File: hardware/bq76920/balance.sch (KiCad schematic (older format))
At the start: 32 parts, among them Q4 NTR3C21NZ, Q5 NTR3C21NZ, Q6 NTR3C21NZ, Q7 NTR3C21NZ, Q8 NTR3C21NZ

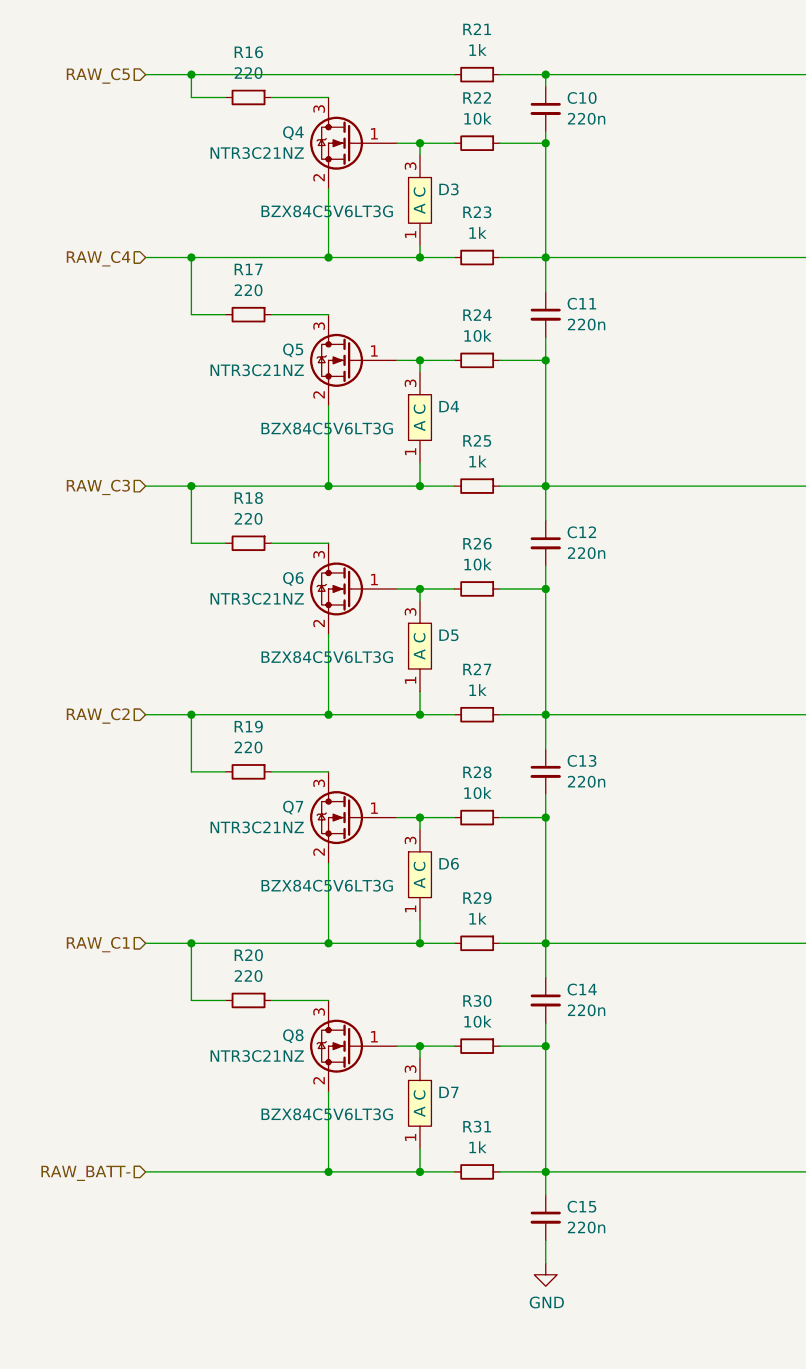
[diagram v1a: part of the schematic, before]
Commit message: update cpu and reduce BOM
Signed-off-by: Ene Alexandru <ene.alexandru@gmail.com>
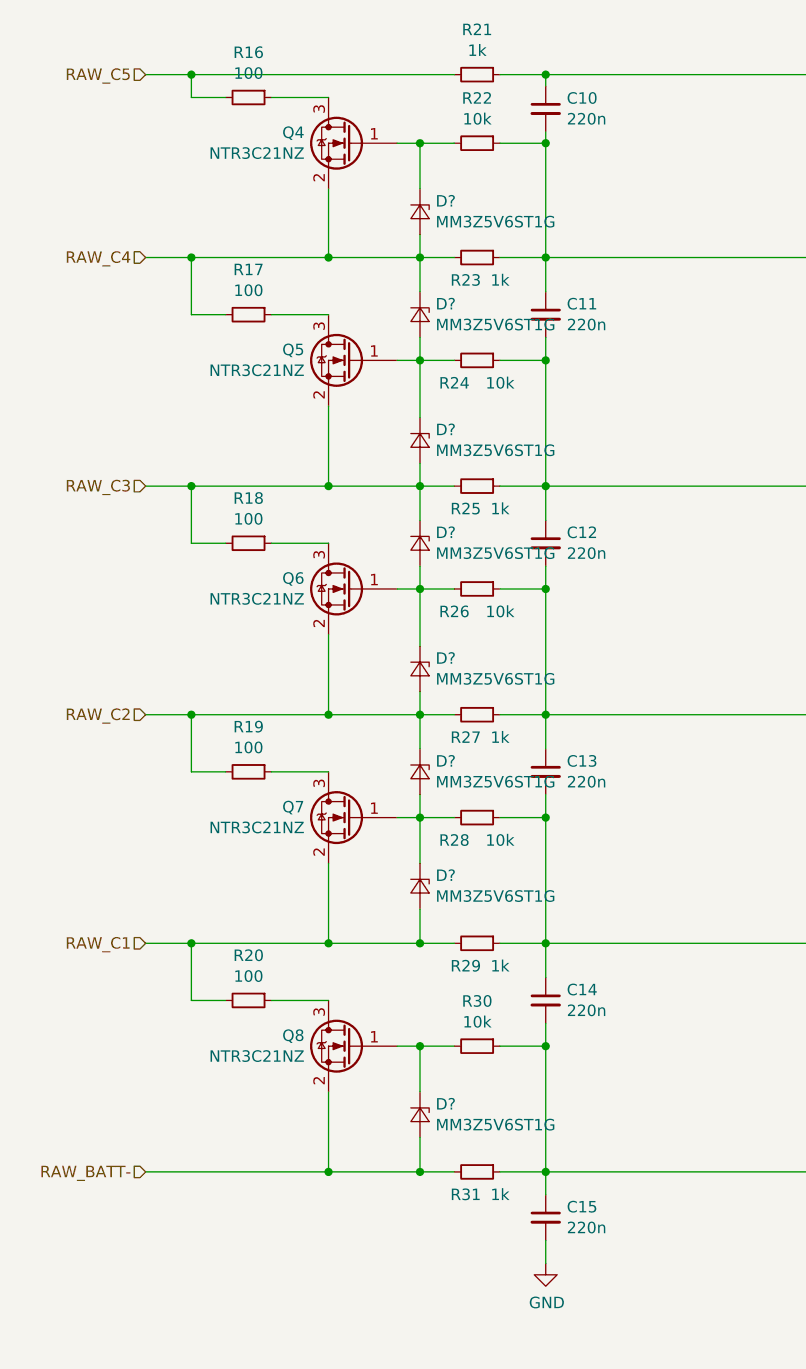
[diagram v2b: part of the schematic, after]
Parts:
- removed D3, D4, D5, D6, D7: BZX84C5V6LT3G, Package_TO_SOT_SMD:SOT-23, symbol bq76920-rescue:BZX84C5V6LT3G-bq769xx
- added D? (x8): MM3Z5V6ST1G, Diode_SMD:D_SOD-323, symbol Device:D_Zener_Small
- R16, R17, R18, R19, R20: value 220 -> 100
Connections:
- net RAW_BATT-: now also D?.2 (A)
- net RAW_C1: now also D?.2 (A)
- net RAW_C2: now also D?.1 (K), D?.2 (A)
- net RAW_C3: now also D?.1 (K), D?.2 (A)
- net RAW_C4: now also D?.1 (K), D?.2 (A)
- net at Q4.1 (G), R22.2: now also D?.1 (K)
- net at Q5.1 (G), R24.2: now also D?.1 (K), D?.2 (A)
- net at Q6.1 (G), R26.2: now also D?.1 (K), D?.2 (A)
- net at Q7.1 (G), R28.2: now also D?.1 (K), D?.2 (A)
- net at Q8.1 (G), R30.2: now also D?.1 (K)
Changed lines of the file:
@@
-$EndComp
-$Comp
-L bq76920-rescue:BZX84C5V6LT3G-bq769xx D3
-U 1 1 5D445057
-P 3700 1200
-AR Path="/5D445057" Ref="D3"  Part="1"
-AR Path="/5D4426A3/5D445057" Ref="D3"  Part="1"
-F 0 "D3" H 3778 1046 50  0000 L CNN
-F 1 "BZX84C5V6LT3G" H 3000 950 50  0000 L CNN
-F 2 "Package_TO_SOT_SMD:SOT-23" H 3700 1200 50  0001 C CNN
-F 3 "" H 3700 1200 50  0001 C CNN
-	1    3700 1200
-	1    0    0    -1
 $EndComp
 $Comp
@@
 P 2950 950
 F 0 "R16" V 2754 950 50  0000 C CNN
-F 1 "220" V 2845 950 50  0000 C CNN
+F 1 "100" V 2845 950 50  0000 C CNN
 F 2 "Resistor_SMD:R_1206_3216Metric_Pad1.42x1.75mm_HandSolder" H 2950 950 50  0001 C CNN
 F 3 "~" H 2950 950 50  0001 C CNN
@@
 U 1 1 5D44C6D5
 P 3950 1650
-F 0 "R23" V 3754 1650 50  0000 C CNN
-F 1 "1k" V 3845 1650 50  0000 C CNN
+F 0 "R23" V 4050 1600 50  0000 C CNN
+F 1 "1k" V 4050 1750 50  0000 C CNN
 F 2 "Resistor_SMD:R_0805_2012Metric_Pad1.15x1.40mm_HandSolder" H 3950 1650 50  0001 C CNN
 F 3 "~" H 3950 1650 50  0001 C CNN
@@
 Wire Wire Line
 	4250 850  4050 850
-Wire Wire Line
-	3700 1600 3700 1650
 Connection ~ 3700 1650
 Wire Wire Line
@@
 Wire Wire Line
 	3600 1150 3700 1150
-Wire Wire Line
-	3700 1150 3700 1200
 Connection ~ 3700 1150
 Wire Wire Line
@@
 P 2950 1900
 F 0 "R17" V 2754 1900 50  0000 C CNN
-F 1 "220" V 2845 1900 50  0000 C CNN
+F 1 "100" V 2845 1900 50  0000 C CNN
 F 2 "Resistor_SMD:R_1206_3216Metric_Pad1.42x1.75mm_HandSolder" H 2950 1900 50  0001 C CNN
 F 3 "~" H 2950 1900 50  0001 C CNN
@@
 $EndComp
 $Comp
-L bq76920-rescue:BZX84C5V6LT3G-bq769xx D4
-U 1 1 5D458C86
-P 3700 2150
-AR Path="/5D458C86" Ref="D4"  Part="1"
-AR Path="/5D4426A3/5D458C86" Ref="D4"  Part="1"
-F 0 "D4" H 3778 1996 50  0000 L CNN
-F 1 "BZX84C5V6LT3G" H 3000 1900 50  0000 L CNN
-F 2 "Package_TO_SOT_SMD:SOT-23" H 3700 2150 50  0001 C CNN
-F 3 "" H 3700 2150 50  0001 C CNN
-	1    3700 2150
-	1    0    0    -1
-$EndComp
-$Comp
 L Device:R_Small R24
 U 1 1 5D4590AC
 P 3950 2100
-F 0 "R24" V 3754 2100 50  0000 C CNN
-F 1 "10k" V 3845 2100 50  0000 C CNN
+F 0 "R24" V 4050 2000 50  0000 C CNN
+F 1 "10k" V 4050 2200 50  0000 C CNN
 F 2 "Resistor_SMD:R_0805_2012Metric_Pad1.15x1.40mm_HandSolder" H 3950 2100 50  0001 C CNN
 F 3 "~" H 3950 2100 50  0001 C CNN
@@
 U 1 1 5D45948A
 P 3950 2650
-F 0 "R25" V 3754 2650 50  0000 C CNN
-F 1 "1k" V 3845 2650 50  0000 C CNN
+F 0 "R25" V 4050 2600 50  0000 C CNN
+F 1 "1k" V 4050 2750 50  0000 C CNN
 F 2 "Resistor_SMD:R_0805_2012Metric_Pad1.15x1.40mm_HandSolder" H 3950 2650 50  0001 C CNN
 F 3 "~" H 3950 2650 50  0001 C CNN
@@
 Wire Wire Line
 	3850 2100 3700 2100
-Wire Wire Line
-	3700 2150 3700 2100
 Connection ~ 3700 2100
 Wire Wire Line
@@
 P 2950 2900
 F 0 "R18" V 2754 2900 50  0000 C CNN
-F 1 "220" V 2845 2900 50  0000 C CNN
+F 1 "100" V 2845 2900 50  0000 C CNN
 F 2 "Resistor_SMD:R_1206_3216Metric_Pad1.42x1.75mm_HandSolder" H 2950 2900 50  0001 C CNN
 F 3 "~" H 2950 2900 50  0001 C CNN
@@
 $EndComp
 $Comp
-L bq76920-rescue:BZX84C5V6LT3G-bq769xx D5
-U 1 1 5D461225
-P 3700 3150
-AR Path="/5D461225" Ref="D5"  Part="1"
-AR Path="/5D4426A3/5D461225" Ref="D5"  Part="1"
-F 0 "D5" H 3778 2996 50  0000 L CNN
-F 1 "BZX84C5V6LT3G" H 3000 2900 50  0000 L CNN
-F 2 "Package_TO_SOT_SMD:SOT-23" H 3700 3150 50  0001 C CNN
-F 3 "" H 3700 3150 50  0001 C CNN
-	1    3700 3150
-	1    0    0    -1
-$EndComp
-$Comp
 L Device:R_Small R26
 U 1 1 5D46299B
 P 3950 3100
-F 0 "R26" V 3754 3100 50  0000 C CNN
-F 1 "10k" V 3845 3100 50  0000 C CNN
+F 0 "R26" V 4050 3000 50  0000 C CNN
+F 1 "10k" V 4050 3200 50  0000 C CNN
 F 2 "Resistor_SMD:R_0805_2012Metric_Pad1.15x1.40mm_HandSolder" H 3950 3100 50  0001 C CNN
 F 3 "~" H 3950 3100 50  0001 C CNN
@@
 U 1 1 5D462DC7
 P 3950 3650
-F 0 "R27" V 3754 3650 50  0000 C CNN
-F 1 "1k" V 3845 3650 50  0000 C CNN
+F 0 "R27" V 4050 3600 50  0000 C CNN
+F 1 "1k" V 4050 3750 50  0000 C CNN
 F 2 "Resistor_SMD:R_0805_2012Metric_Pad1.15x1.40mm_HandSolder" H 3950 3650 50  0001 C CNN
 F 3 "~" H 3950 3650 50  0001 C CNN
@@
 Wire Wire Line
 	3850 3100 3700 3100
-Wire Wire Line
-	3700 3150 3700 3100
 Connection ~ 3700 3100
 Wire Wire Line
@@
 P 2950 3900
 F 0 "R19" V 2754 3900 50  0000 C CNN
-F 1 "220" V 2845 3900 50  0000 C CNN
+F 1 "100" V 2845 3900 50  0000 C CNN
 F 2 "Resistor_SMD:R_1206_3216Metric_Pad1.42x1.75mm_HandSolder" H 2950 3900 50  0001 C CNN
 F 3 "~" H 2950 3900 50  0001 C CNN
@@
 $EndComp
 $Comp
-L bq76920-rescue:BZX84C5V6LT3G-bq769xx D6
-U 1 1 5D47B43C
-P 3700 4150
-AR Path="/5D47B43C" Ref="D6"  Part="1"
-AR Path="/5D4426A3/5D47B43C" Ref="D6"  Part="1"
-F 0 "D6" H 3778 3996 50  0000 L CNN
-F 1 "BZX84C5V6LT3G" H 3000 3900 50  0000 L CNN
-F 2 "Package_TO_SOT_SMD:SOT-23" H 3700 4150 50  0001 C CNN
-F 3 "" H 3700 4150 50  0001 C CNN
-	1    3700 4150
-	1    0    0    -1
-$EndComp
-$Comp
 L Device:R_Small R28
 U 1 1 5D47B896
 P 3950 4100
-F 0 "R28" V 3754 4100 50  0000 C CNN
-F 1 "10k" V 3845 4100 50  0000 C CNN
+F 0 "R28" V 4050 4000 50  0000 C CNN
+F 1 "10k" V 4050 4200 50  0000 C CNN
 F 2 "Resistor_SMD:R_0805_2012Metric_Pad1.15x1.40mm_HandSolder" H 3950 4100 50  0001 C CNN
 F 3 "~" H 3950 4100 50  0001 C CNN
@@
 U 1 1 5D47BD30
 P 3950 4650
-F 0 "R29" V 3754 4650 50  0000 C CNN
-F 1 "1k" V 3845 4650 50  0000 C CNN
+F 0 "R29" V 4050 4600 50  0000 C CNN
+F 1 "1k" V 4050 4750 50  0000 C CNN
 F 2 "Resistor_SMD:R_0805_2012Metric_Pad1.15x1.40mm_HandSolder" H 3950 4650 50  0001 C CNN
 F 3 "~" H 3950 4650 50  0001 C CNN
@@
 Wire Wire Line
 	3300 4650 2700 4650
-Wire Wire Line
-	3700 4550 3700 4650
 Connection ~ 3700 4650
 Wire Wire Line
@@
 Wire Wire Line
 	3600 4100 3700 4100
-Wire Wire Line
-	3700 4150 3700 4100
 Connection ~ 3700 4100
 Wire Wire Line
@@
 P 2950 4900
 F 0 "R20" V 2754 4900 50  0000 C CNN
-F 1 "220" V 2845 4900 50  0000 C CNN
+F 1 "100" V 2845 4900 50  0000 C CNN
 F 2 "Resistor_SMD:R_1206_3216Metric_Pad1.42x1.75mm_HandSolder" H 2950 4900 50  0001 C CNN
 F 3 "~" H 2950 4900 50  0001 C CNN
@@
 $EndComp
 $Comp
-L bq76920-rescue:BZX84C5V6LT3G-bq769xx D7
-U 1 1 5D493241
-P 3700 5150
-AR Path="/5D493241" Ref="D7"  Part="1"
-AR Path="/5D4426A3/5D493241" Ref="D7"  Part="1"
-F 0 "D7" H 3778 4996 50  0000 L CNN
-F 1 "BZX84C5V6LT3G" H 3000 4900 50  0000 L CNN
-F 2 "Package_TO_SOT_SMD:SOT-23" H 3700 5150 50  0001 C CNN
-F 3 "" H 3700 5150 50  0001 C CNN
-	1    3700 5150
-	1    0    0    -1
-$EndComp
-$Comp
 L Device:R_Small R30
 U 1 1 5D493619
@@
 U 1 1 5D493A41
 P 3950 5650
-F 0 "R31" V 3754 5650 50  0000 C CNN
-F 1 "1k" V 3845 5650 50  0000 C CNN
+F 0 "R31" V 4050 5600 50  0000 C CNN
+F 1 "1k" V 4050 5750 50  0000 C CNN
 F 2 "Resistor_SMD:R_0805_2012Metric_Pad1.15x1.40mm_HandSolder" H 3950 5650 50  0001 C CNN
 F 3 "~" H 3950 5650 50  0001 C CNN
@@
 Wire Wire Line
 	3850 5650 3700 5650
-Wire Wire Line
-	3700 5550 3700 5650
 Connection ~ 3700 5650
 Wire Wire Line
@@
 Wire Wire Line
 	3600 5100 3700 5100
-Wire Wire Line
-	3700 5150 3700 5100
 Connection ~ 3700 5100
 Wire Wire Line
@@
 Text Notes 7400 7500 0    50   ~ 0
 cell balance section
+$Comp
+L Device:D_Zener_Small D?
+U 1 1 5E152DFD
+P 3700 1450
+F 0 "D?" V 3654 1518 50  0000 L CNN
+F 1 "MM3Z5V6ST1G" V 3745 1518 50  0000 L CNN
+F 2 "Diode_SMD:D_SOD-323" V 3700 1450 50  0001 C CNN
+F 3 "~" V 3700 1450 50  0001 C CNN
+	1    3700 1450
+	0    1    1    0
+$EndComp
+$Comp
+L Device:D_Zener_Small D?
+U 1 1 5E1532E1
+P 3700 1900
+F 0 "D?" V 3654 1968 50  0000 L CNN
+F 1 "MM3Z5V6ST1G" V 3745 1968 50  0000 L CNN
+F 2 "Diode_SMD:D_SOD-323" V 3700 1900 50  0001 C CNN
+F 3 "~" V 3700 1900 50  0001 C CNN
+	1    3700 1900
+	0    1    1    0
+$EndComp
+$Comp
+L Device:D_Zener_Small D?
+U 1 1 5E1533AC
+P 3700 2450
+F 0 "D?" V 3654 2518 50  0000 L CNN
+F 1 "MM3Z5V6ST1G" V 3745 2518 50  0000 L CNN
+F 2 "Diode_SMD:D_SOD-323" V 3700 2450 50  0001 C CNN
+F 3 "~" V 3700 2450 50  0001 C CNN
+	1    3700 2450
+	0    1    1    0
+$EndComp
+$Comp
+L Device:D_Zener_Small D?
+U 1 1 5E153406
+P 3700 2900
+F 0 "D?" V 3654 2968 50  0000 L CNN
+F 1 "MM3Z5V6ST1G" V 3745 2968 50  0000 L CNN
+F 2 "Diode_SMD:D_SOD-323" V 3700 2900 50  0001 C CNN
+F 3 "~" V 3700 2900 50  0001 C CNN
+	1    3700 2900
+	0    1    1    0
+$EndComp
+$Comp
+L Device:D_Zener_Small D?
+U 1 1 5E15346A
+P 3700 3900
+F 0 "D?" V 3654 3968 50  0000 L CNN
+F 1 "MM3Z5V6ST1G" V 3745 3968 50  0000 L CNN
+F 2 "Diode_SMD:D_SOD-323" V 3700 3900 50  0001 C CNN
+F 3 "~" V 3700 3900 50  0001 C CNN
+	1    3700 3900
+	0    1    1    0
+$EndComp
+$Comp
+L Device:D_Zener_Small D?
+U 1 1 5E1535C6
+P 3700 4400
+F 0 "D?" V 3654 4468 50  0000 L CNN
+F 1 "MM3Z5V6ST1G" V 3745 4468 50  0000 L CNN
+F 2 "Diode_SMD:D_SOD-323" V 3700 4400 50  0001 C CNN
+F 3 "~" V 3700 4400 50  0001 C CNN
+	1    3700 4400
+	0    1    1    0
+$EndComp
+$Comp
+L Device:D_Zener_Small D?
+U 1 1 5E153630
+P 3700 5400
+F 0 "D?" V 3654 5468 50  0000 L CNN
+F 1 "MM3Z5V6ST1G" V 3745 5468 50  0000 L CNN
+F 2 "Diode_SMD:D_SOD-323" V 3700 5400 50  0001 C CNN
+F 3 "~" V 3700 5400 50  0001 C CNN
+	1    3700 5400
+	0    1    1    0
+$EndComp
+Wire Wire Line
+	3700 5500 3700 5650
+Wire Wire Line
+	3700 5100 3700 5300
+Wire Wire Line
+	3700 4500 3700 4650
+Wire Wire Line
+	3700 4100 3700 4300
+Wire Wire Line
+	3700 4000 3700 4100
+Wire Wire Line
+	3700 3800 3700 3650
+$Comp
+L Device:D_Zener_Small D?
+U 1 1 5E16355C
+P 3700 3450
+F 0 "D?" V 3654 3518 50  0000 L CNN
+F 1 "MM3Z5V6ST1G" V 3745 3518 50  0000 L CNN
+F 2 "Diode_SMD:D_SOD-323" V 3700 3450 50  0001 C CNN
+F 3 "~" V 3700 3450 50  0001 C CNN
+	1    3700 3450
+	0    1    1    0
+$EndComp
+Wire Wire Line
+	3700 3100 3700 3350
+Wire Wire Line
+	3700 3000 3700 3100
+Wire Wire Line
+	3700 2800 3700 2650
+Wire Wire Line
+	3700 2100 3700 2350
+Wire Wire Line
+	3700 2000 3700 2100
+Wire Wire Line
+	3700 1800 3700 1650
+Wire Wire Line
+	3700 1550 3700 1650
+Wire Wire Line
+	3700 1150 3700 1350
 $EndSCHEMATC
